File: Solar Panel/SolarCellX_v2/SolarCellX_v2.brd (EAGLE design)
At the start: 100 x 78 mm, 17 parts

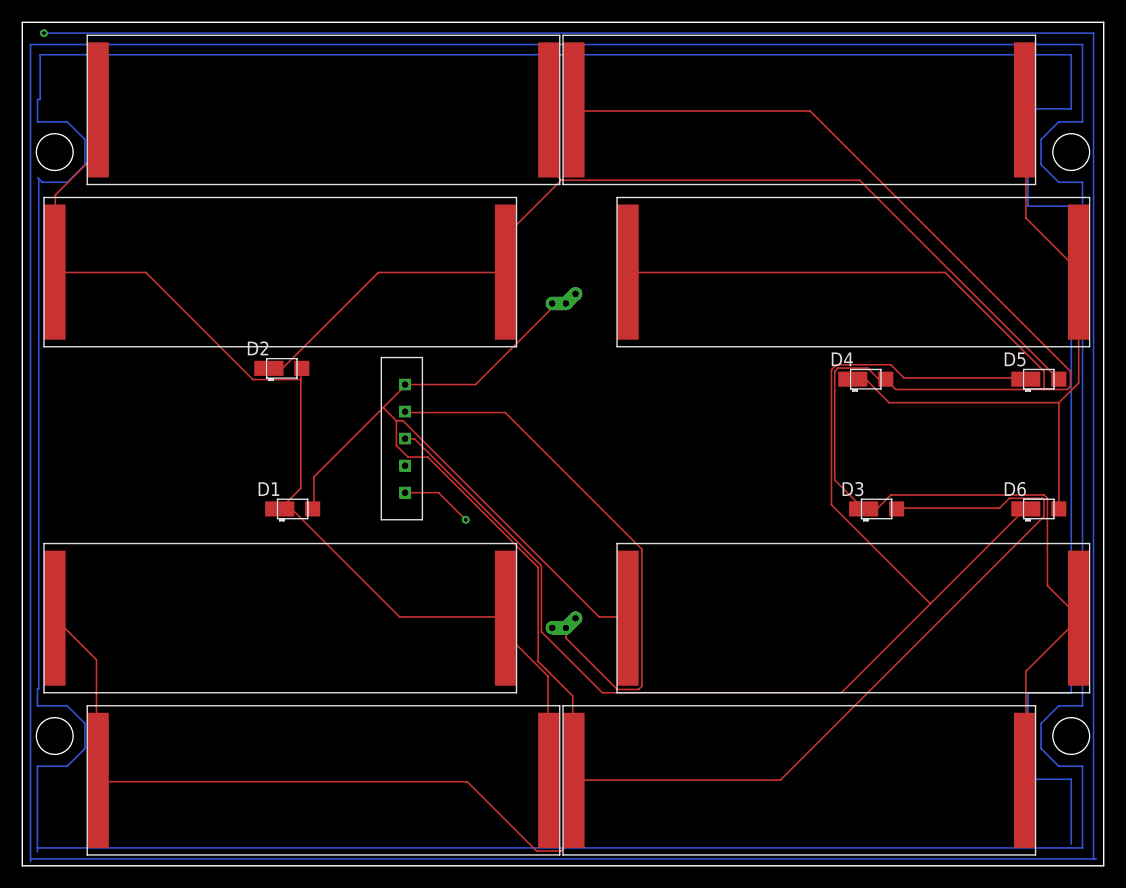
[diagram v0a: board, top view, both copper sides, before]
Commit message: Edits to Solar cell
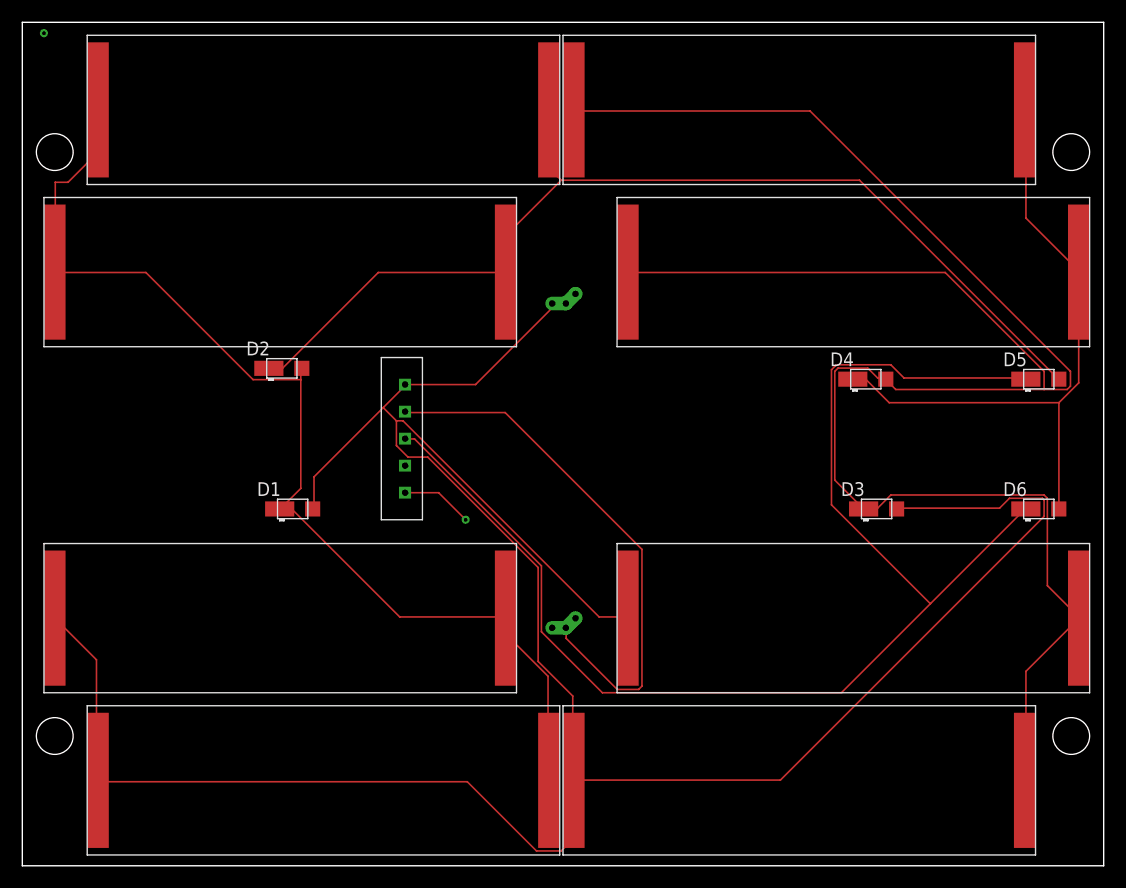
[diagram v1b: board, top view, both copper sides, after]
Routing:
- net N$1: track 899.9 -> 0.00 mm
- net N$2: track 99.6 -> 100.3 mm
